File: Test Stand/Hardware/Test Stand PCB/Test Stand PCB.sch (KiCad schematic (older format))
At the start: 18 parts, among them J1 Screw_Terminal_01x02, J2 Screw_Terminal_01x02, J3 Screw_Terminal_01x02, J4 Screw_Terminal_01x04, J5 Screw_Terminal_01x02, U1 AdafruitHuzzah32Breakout, U2 Adafruit_MAX31856, U3 Adafruit_MAX31856, U4 Adafruit_MAX31856, U5 Adafruit_MAX31856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

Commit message: Update file names and upload of the schematic template
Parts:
- ADC1: symbol Breakout_Test_Bench_Library:Adafruit_ADS1115 -> Test_Stand_Symbol_Library:Adafruit_ADS1115
- ADC2: symbol Breakout_Test_Bench_Library:Adafruit_ADS1015 -> Test_Stand_Symbol_Library:Adafruit_ADS1015
- U1: symbol Breakout_Test_Bench_Library:AdafruitHuzzah32Breakout -> Test_Stand_Symbol_Library:AdafruitHuzzah32Breakout
- U2, U5: symbol Breakout_Test_Bench_Library:Adafruit_MAX31856 -> Test_Stand_Symbol_Library:Adafruit_MAX31856
- U3: renamed from U4; symbol Breakout_Test_Bench_Library:Adafruit_MAX31856 -> Test_Stand_Symbol_Library:Adafruit_MAX31856
- U4: renamed from U3; symbol Breakout_Test_Bench_Library:Adafruit_MAX31856 -> Test_Stand_Symbol_Library:Adafruit_MAX31856
- U7: symbol Breakout_Test_Bench_Library:INA_122P -> Test_Stand_Symbol_Library:INA_122P
- U8: symbol Breakout_Test_Bench_Library:Adafruit_MicroSD_Breakout -> Test_Stand_Symbol_Library:Adafruit_MicroSD_Breakout
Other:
- moved on the sheet: J1, J2, J3, J5, R1, R2, R3

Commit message: Updated Test schematic and PCB Design
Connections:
- net labels removed: +3.3V
- wire segments 44 -> 43
- no-connect marks 32 -> 33
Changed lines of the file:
@@
 Text GLabel 2500 6300 2    50   Input ~ 0
 CS_2
-Text GLabel 2500 6100 2    50   Input ~ 0
-CS_4
 Text GLabel 2500 6000 2    50   Input ~ 0
+CS_3
+Text GLabel 2500 6200 2    50   Input ~ 0
 CS_5
-Text GLabel 2500 6200 2    50   Input ~ 0
-CS_3
 Wire Wire Line
 	2500 5700 2650 5700
@@
 NoConn ~ 1600 5900
 NoConn ~ 1600 6000
-NoConn ~ 1600 6600
 NoConn ~ 2500 5800
 $Comp
@@
 Wire Wire Line
 	5400 6750 5650 6750
-$Comp
-L power:+3.3V #PWR0133
-U 1 1 5F8FE92E
-P 1300 5200
-F 0 "#PWR0133" H 1300 5050 50  0001 C CNN
-F 1 "+3.3V" V 1315 5328 50  0000 L CNN
-F 2 "" H 1300 5200 50  0001 C CNN
-F 3 "" H 1300 5200 50  0001 C CNN
-	1    1300 5200
-	0    -1   -1   0
-$EndComp
-Wire Wire Line
-	1300 5200 1600 5200
-$Comp
-L power:+3.3V #PWR0134
-U 1 1 5F8FFEBE
-P 5600 6650
-F 0 "#PWR0134" H 5600 6500 50  0001 C CNN
-F 1 "+3.3V" V 5615 6778 50  0000 L CNN
-F 2 "" H 5600 6650 50  0001 C CNN
-F 3 "" H 5600 6650 50  0001 C CNN
-	1    5600 6650
-	0    1    1    0
-$EndComp
-Wire Wire Line
-	5400 6650 5600 6650
-NoConn ~ 5400 6550
 NoConn ~ 5400 7250
 Wire Notes Line
@@
 	10050 5550 10400 5550
 $Comp
-L power:+12V #PWR?
+L power:+12V #PWR0114
 U 1 1 5FB4126D
 P 10400 5550
-F 0 "#PWR?" H 10400 5400 50  0001 C CNN
+F 0 "#PWR0114" H 10400 5400 50  0001 C CNN
 F 1 "+12V" H 10415 5723 50  0000 C CNN
 F 2 "" H 10400 5550 50  0001 C CNN
@@
 	10400 5550 10550 5550
 $Comp
-L power:+12V #PWR?
+L power:+12V #PWR0115
 U 1 1 5FB42063
 P 8350 6250
-F 0 "#PWR?" H 8350 6100 50  0001 C CNN
+F 0 "#PWR0115" H 8350 6100 50  0001 C CNN
 F 1 "+12V" H 8365 6423 50  0000 C CNN
 F 2 "" H 8350 6250 50  0001 C CNN
@@
 $EndComp
 $Comp
-L power:+12V #PWR?
+L power:+12V #PWR0124
 U 1 1 5FB428B7
 P 8350 5500
-F 0 "#PWR?" H 8350 5350 50  0001 C CNN
+F 0 "#PWR0124" H 8350 5350 50  0001 C CNN
 F 1 "+12V" H 8365 5673 50  0000 C CNN
 F 2 "" H 8350 5500 50  0001 C CNN
@@
 $EndComp
 $Comp
-L power:+12V #PWR?
+L power:+12V #PWR0126
 U 1 1 5FB42C6F
 P 8350 4750
-F 0 "#PWR?" H 8350 4600 50  0001 C CNN
+F 0 "#PWR0126" H 8350 4600 50  0001 C CNN
 F 1 "+12V" H 8365 4923 50  0000 C CNN
 F 2 "" H 8350 4750 50  0001 C CNN
@@
 	1    0    0    -1
 $EndComp
+Text GLabel 1600 6600 0    50   Input ~ 0
+CS_4
+NoConn ~ 2500 6100
+$Comp
+L power:+5V #PWR?
+U 1 1 5FBF3CC9
+P 5600 6550
+F 0 "#PWR?" H 5600 6400 50  0001 C CNN
+F 1 "+5V" V 5615 6678 50  0000 L CNN
+F 2 "" H 5600 6550 50  0001 C CNN
+F 3 "" H 5600 6550 50  0001 C CNN
+	1    5600 6550
+	0    1    1    0
+$EndComp
+Wire Wire Line
+	5400 6550 5600 6550
+NoConn ~ 5400 6650
+NoConn ~ 1600 5200
 $EndSCHEMATC

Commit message: Added gerber file for manufacturing of Test Stand PCB v1.0
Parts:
- added D1: D_Schottky, Diode_THT:D_DO-41_SOD81_P7.62mm_Horizontal, symbol Device:D_Schottky
- added J6: Screw_Terminal_01x02, TerminalBlock:TerminalBlock_bornier-2_P5.08mm, symbol Connector:Screw_Terminal_01x02
- added Q1: Q_NMOS_GDS, Package_TO_SOT_THT:TO-251-3_Vertical, symbol Device:Q_NMOS_GDS
- added R5: 100, Resistor_THT:R_Axial_DIN0204_L3.6mm_D1.6mm_P5.08mm_Horizontal, symbol Device:R
- added R6: 10k, Resistor_THT:R_Axial_DIN0204_L3.6mm_D1.6mm_P5.08mm_Horizontal, symbol Device:R
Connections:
- net +12V: now also D1.1 (K), J6.1 (Pin_1)
- net CS_3: now also U1.22 (D33); no longer U1.23 (D27)
- net GND: now also Q1.3 (S), R6.2
- new net: Q1.1 (G), R5.1, R6.1
- new net: D1.2 (A), J6.2 (Pin_2), Q1.2 (D)
- new net Gate_Pin: R5.2, U1.23 (D27)
- no-connect marks 33 -> 32
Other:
- note added: "Solenoid Valve Driver Circuit\n"
- moved on the sheet: U2, U3, U4, U5

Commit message: Updated Schematic PDF
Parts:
- ADC1: symbol Test_Stand_Symbol_Library:Adafruit_ADS1115 -> Test-Stand-PCB-rescue:Adafruit_ADS1115-Test_Stand_Symbol_Library
- ADC2: symbol Test_Stand_Symbol_Library:Adafruit_ADS1015 -> Test-Stand-PCB-rescue:Adafruit_ADS1015-Test_Stand_Symbol_Library
- U1: symbol Test_Stand_Symbol_Library:AdafruitHuzzah32Breakout -> Test-Stand-PCB-rescue:AdafruitHuzzah32Breakout-Test_Stand_Symbol_Library
- U2, U3, U4, U5: symbol Test_Stand_Symbol_Library:Adafruit_MAX31856 -> Test-Stand-PCB-rescue:Adafruit_MAX31856-Test_Stand_Symbol_Library
- U7: symbol Test_Stand_Symbol_Library:INA_122P -> Test-Stand-PCB-rescue:INA_122P-Test_Stand_Symbol_Library
- U8: symbol Test_Stand_Symbol_Library:Adafruit_MicroSD_Breakout -> Test-Stand-PCB-rescue:Adafruit_MicroSD_Breakout-Test_Stand_Symbol_Library
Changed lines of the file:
@@
 $EndDescr
 $Comp
-L Test_Stand_Symbol_Library:Adafruit_ADS1115 ADC1
+L Test-Stand-PCB-rescue:Adafruit_ADS1115-Test_Stand_Symbol_Library ADC1
 U 1 1 5F89A5C4
 P 2400 1350
@@
 $EndComp
 $Comp
-L Test_Stand_Symbol_Library:Adafruit_ADS1015 ADC2
+L Test-Stand-PCB-rescue:Adafruit_ADS1015-Test_Stand_Symbol_Library ADC2
 U 1 1 5F89AD1E
 P 2400 2750
@@
 	2500 3400 2400 3400
 $Comp
-L Test_Stand_Symbol_Library:INA_122P U7
+L Test-Stand-PCB-rescue:INA_122P-Test_Stand_Symbol_Library U7
 U 1 1 5F8AD66F
 P 5250 4850
@@
 $EndComp
 $Comp
-L Test_Stand_Symbol_Library:Adafruit_MAX31856 U5
+L Test-Stand-PCB-rescue:Adafruit_MAX31856-Test_Stand_Symbol_Library U5
 U 1 1 5F8AB18D
 P 7150 2850
@@
 $EndComp
 $Comp
-L Test_Stand_Symbol_Library:Adafruit_MAX31856 U3
+L Test-Stand-PCB-rescue:Adafruit_MAX31856-Test_Stand_Symbol_Library U3
 U 1 1 5F8AB175
 P 7150 1550
@@
 $EndComp
 $Comp
-L Test_Stand_Symbol_Library:Adafruit_MAX31856 U4
+L Test-Stand-PCB-rescue:Adafruit_MAX31856-Test_Stand_Symbol_Library U4
 U 1 1 5F8A86F2
 P 5750 2850
@@
 $EndComp
 $Comp
-L Test_Stand_Symbol_Library:Adafruit_MAX31856 U2
+L Test-Stand-PCB-rescue:Adafruit_MAX31856-Test_Stand_Symbol_Library U2
 U 1 1 5F8A1A33
 P 5750 1550
@@
 Load Cell Amplification Section\n
 $Comp
-L Test_Stand_Symbol_Library:Adafruit_MicroSD_Breakout U8
+L Test-Stand-PCB-rescue:Adafruit_MicroSD_Breakout-Test_Stand_Symbol_Library U8
 U 1 1 5F8F764B
 P 5100 6900
@@
 	6970 6540 6970 6840
 $Comp
-L Test_Stand_Symbol_Library:AdafruitHuzzah32Breakout U1
+L Test-Stand-PCB-rescue:AdafruitHuzzah32Breakout-Test_Stand_Symbol_Library U1
 U 1 1 5F7A20EC
 P 2050 5200

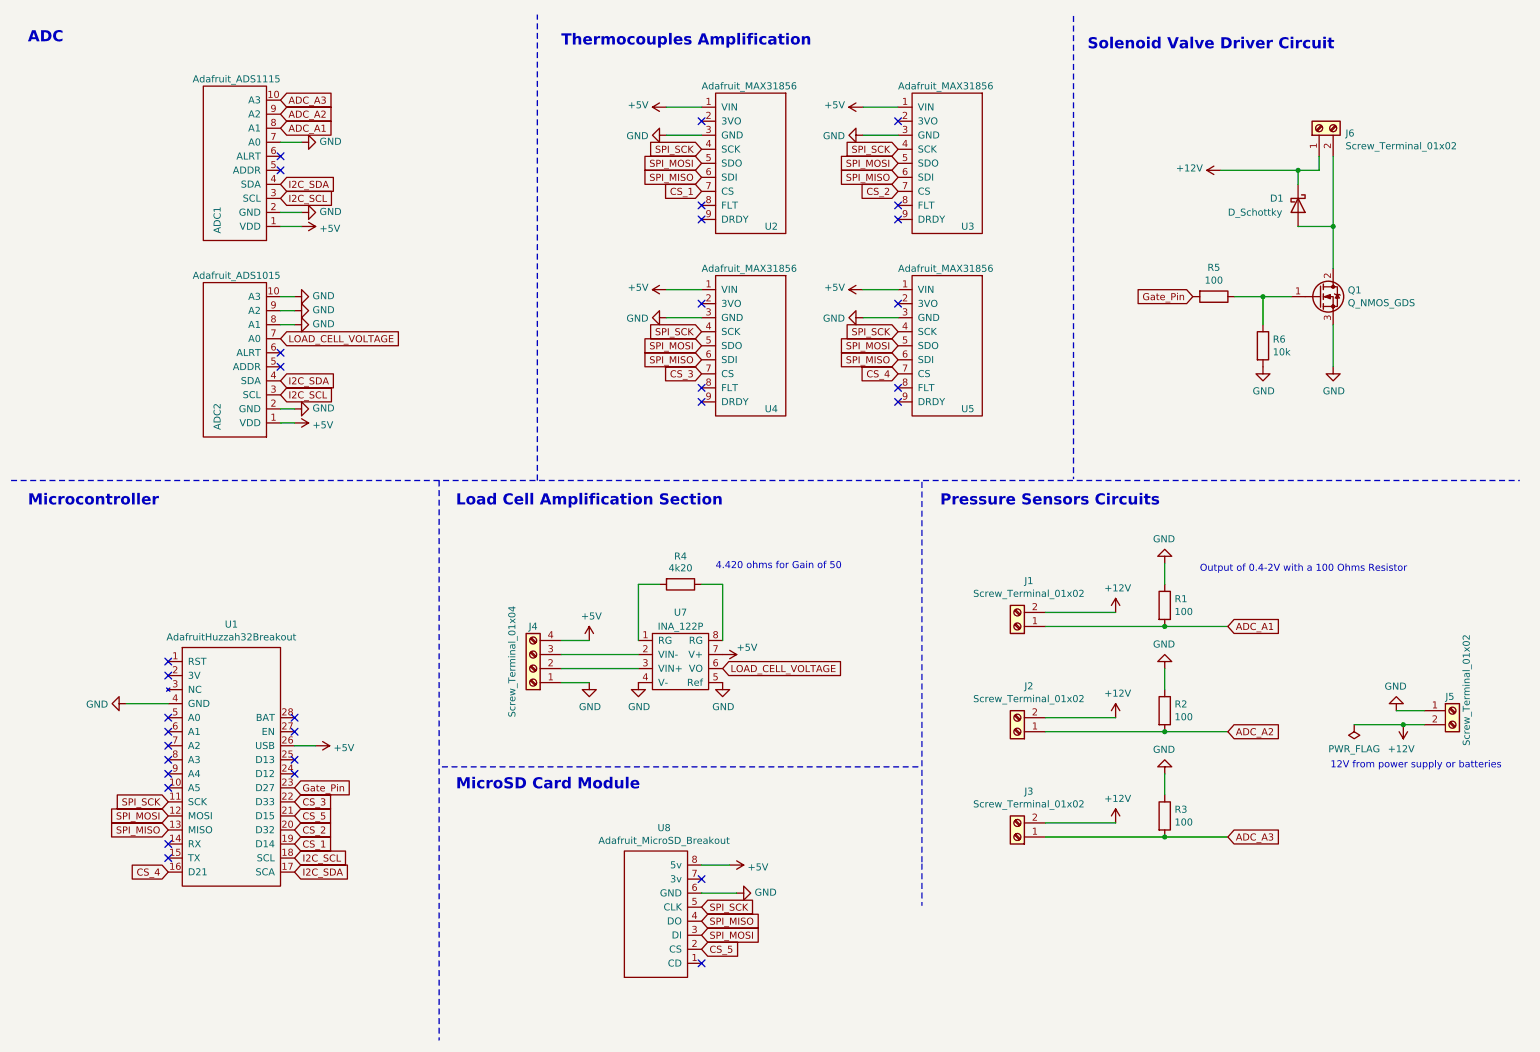
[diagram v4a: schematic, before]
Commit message: Uploading of the Rev1.1 Board
Rev1.1 Board, changes:
- Added 2 more Electronic actuator circuit drivers
- Changed screw terminal layout
- Added Front and Back Silckscreen
- Improved Layout
- Changed resistor footprint
- Changed Sensor Power from 12V to 24V
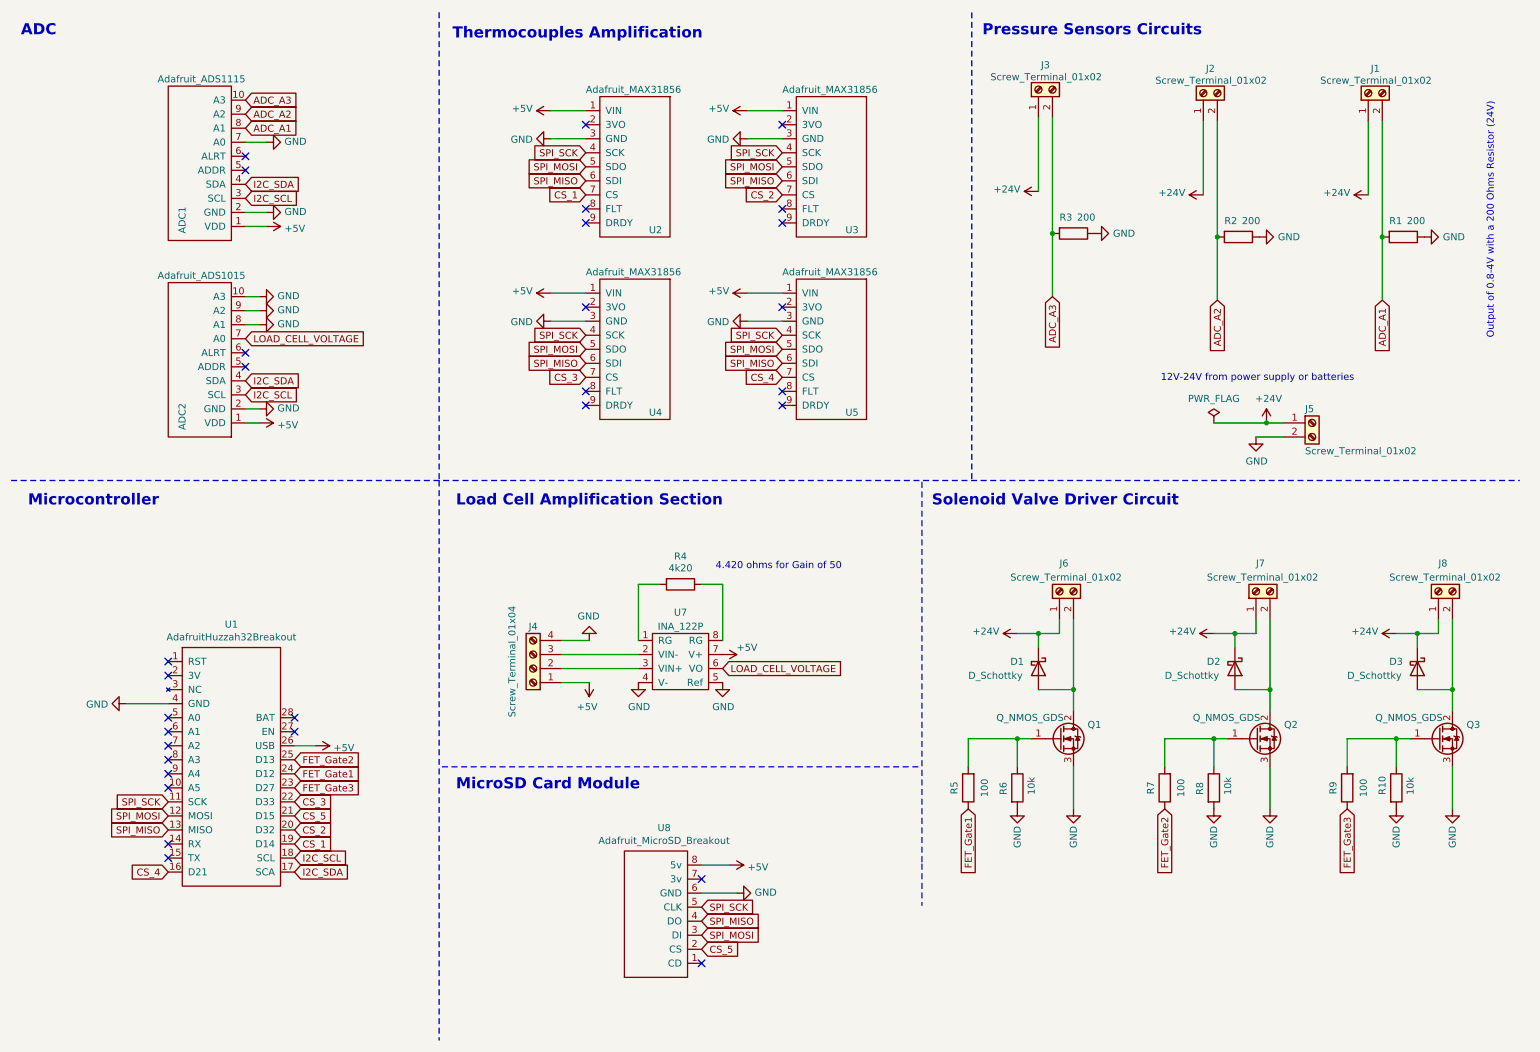
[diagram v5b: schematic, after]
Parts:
- added D2, D3: D_Schottky, Diode_THT:D_DO-41_SOD81_P7.62mm_Horizontal, symbol Device:D_Schottky
- added J7, J8: Screw_Terminal_01x02, TerminalBlock:TerminalBlock_bornier-2_P5.08mm, symbol Connector:Screw_Terminal_01x02
- added Q2, Q3: Q_NMOS_GDS, Package_TO_SOT_THT:TO-251-3_Vertical, symbol Device:Q_NMOS_GDS
- added R10, R8: 10k, Resistor_THT:R_Axial_DIN0204_L3.6mm_D1.6mm_P7.62mm_Horizontal, symbol Device:R
- added R7, R9: 100, Resistor_THT:R_Axial_DIN0204_L3.6mm_D1.6mm_P7.62mm_Horizontal, symbol Device:R
- ADC1: footprint Test Bench PCB Breakout:Adafruit_ADS1115 -> Test Stand PCB Breakout:Adafruit_ADS1115
- ADC2: footprint Test Bench PCB Breakout:Adafruit_ADS1015 -> Test Stand PCB Breakout:Adafruit_ADS1015
- R1, R2, R3: value 100 -> 200; footprint Resistor_THT:R_Axial_DIN0204_L3.6mm_D1.6mm_P5.08mm_Horizontal -> Resistor_THT:R_Axial_DIN0204_L3.6mm_D1.6mm_P7.62mm_Horizontal
- R4, R5, R6: footprint Resistor_THT:R_Axial_DIN0204_L3.6mm_D1.6mm_P5.08mm_Horizontal -> Resistor_THT:R_Axial_DIN0204_L3.6mm_D1.6mm_P7.62mm_Horizontal
- U1: footprint Test Bench PCB Breakout:Adafruit_Huzzah32 -> Test Stand PCB Breakout:Adafruit_Huzzah32
- U2, U3, U4, U5: footprint Test Bench PCB Breakout:Adafruit_MAX31856 -> Test Stand PCB Breakout:Adafruit_MAX31856
- U7: footprint Test Bench PCB Breakout:INA_122P -> Test Stand PCB Breakout:INA_122P
- U8: footprint Test Bench PCB Breakout:Adafruit_MicroSD -> Test Stand PCB Breakout:Adafruit_MicroSD
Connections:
- net +5V: now also J4.1 (Pin_1); no longer J4.4 (Pin_4)
- net ADC_A1: now also J1.2 (Pin_2); no longer J1.1 (Pin_1)
- net ADC_A2: now also J2.2 (Pin_2); no longer J2.1 (Pin_1)
- net ADC_A3: now also J3.2 (Pin_2); no longer J3.1 (Pin_1)
- net GND: now also J4.4 (Pin_4), J5.2 (Pin_2), Q2.3 (S), Q3.3 (S), R10.2, R8.2; no longer J4.1 (Pin_1), J5.1 (Pin_1)
- net FET_Gate1: now reaches U1.24 (D12)
- net FET_Gate1: now also R5.1
- net FET_Gate2: now reaches U1.25 (D13)
- net FET_Gate2: now also R7.1
- net at Q1.1 (G), R6.1: now also R5.2; no longer R5.1
- removed net +12V: D1.1 (K), J1.2 (Pin_2), J2.2 (Pin_2), J3.2 (Pin_2), J5.2 (Pin_2), J6.1 (Pin_1)
- net Gate_Pin renamed FET_Gate3
- net FET_Gate3: now also R9.1; no longer R5.2
- new net: Q2.1 (G), R7.2, R8.1
- new net: D2.2 (A), J7.2 (Pin_2), Q2.2 (D)
- new net: Q3.1 (G), R10.1, R9.2
- new net: D3.2 (A), J8.2 (Pin_2), Q3.2 (D)
- new net +24V: D1.1 (K), D2.1 (K), D3.1 (K), J1.1 (Pin_1), J2.1 (Pin_1), J3.1 (Pin_1), J5.1 (Pin_1), J6.1 (Pin_1), J7.1 (Pin_1), J8.1 (Pin_1)
- no-connect marks 32 -> 30
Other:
- note added: "12V-24V from power supply or batteries\n\n"
- note added: "Output of 0.8-4V with a 200 Ohms Resistor (24V)\n"
- note removed: "12V from power supply or batteries\n\n"
- note removed: "Output of 0.4-2V with a 100 Ohms Resistor\n\n"
- moved on the sheet: ADC1, ADC2, D1, J3, J5, J6, Q1, R5, R6, U2, U3, U4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
